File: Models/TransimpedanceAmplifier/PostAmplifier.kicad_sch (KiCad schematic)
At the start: 18 parts, among them J1 Conn_01x02_Pin, J7 Conn_01x02_Pin, J8 Conn_01x02_Pin, Q3 Q_PNP, Q4 Q_NPN, U6 OP37G

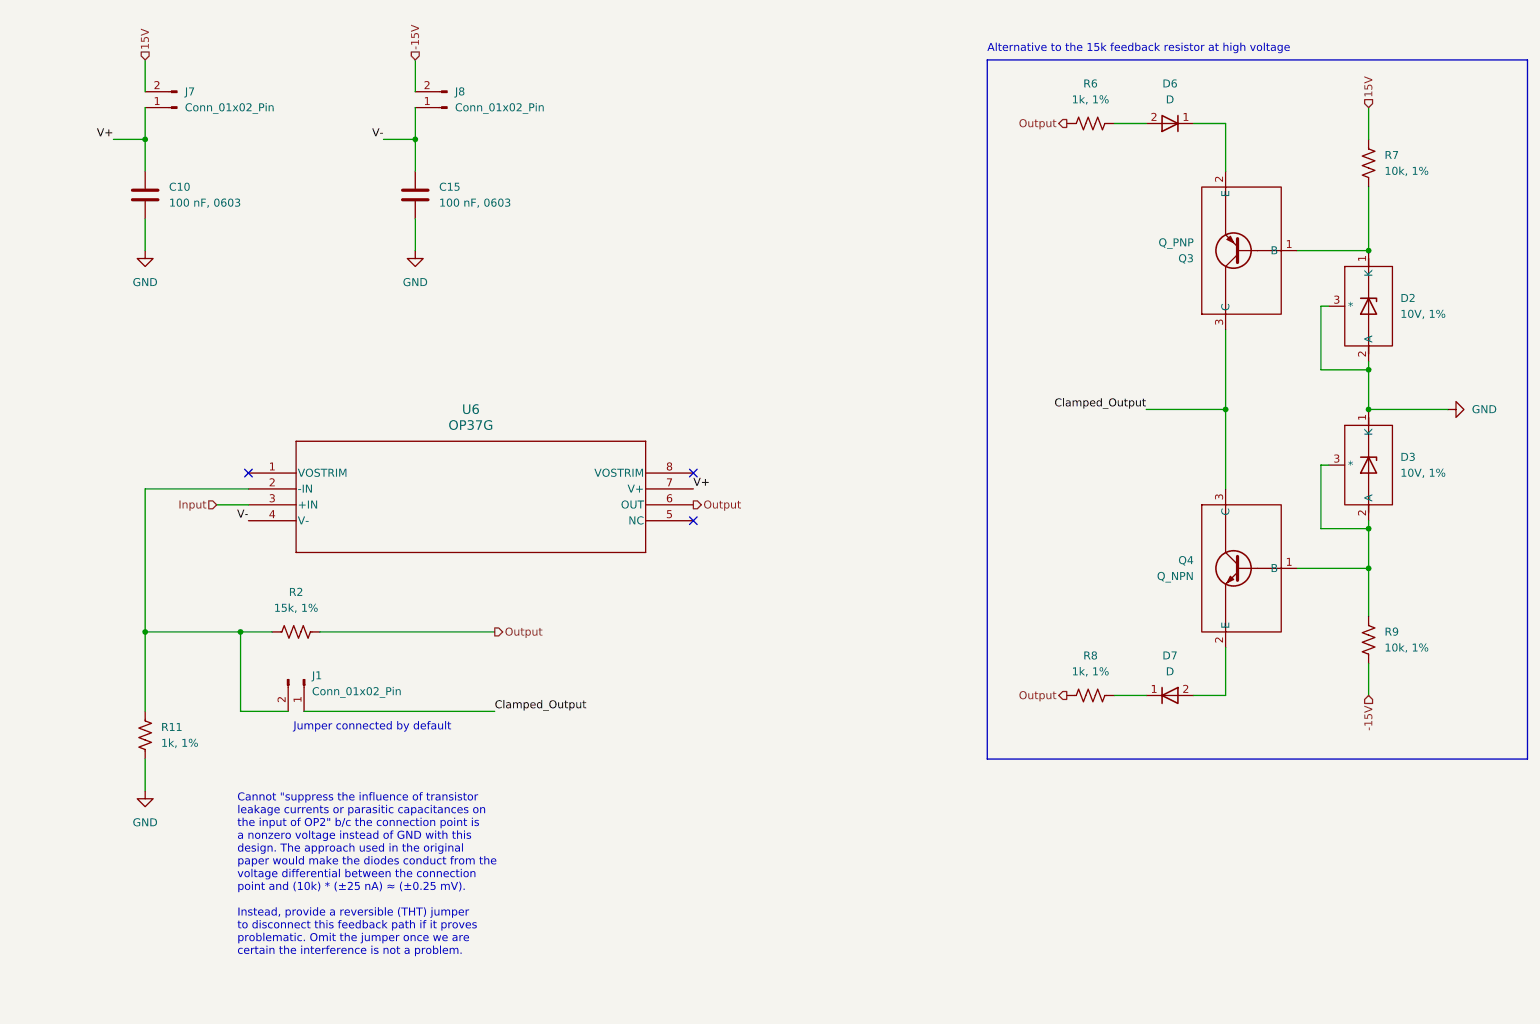
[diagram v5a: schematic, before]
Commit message: Overhauled all of the annotations
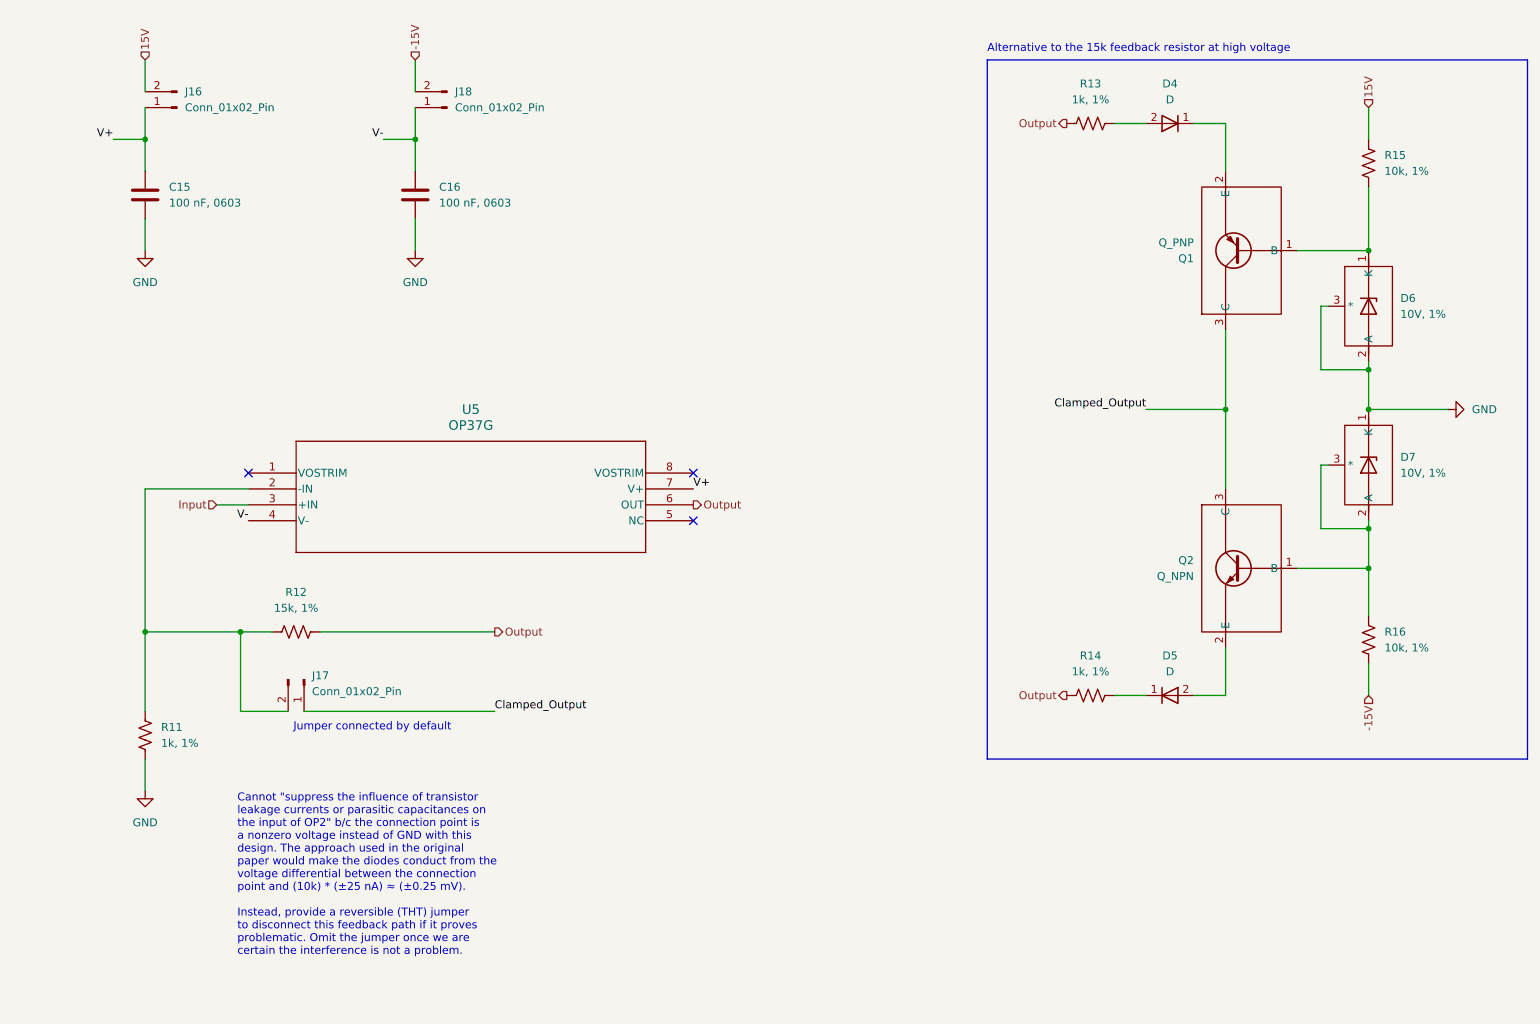
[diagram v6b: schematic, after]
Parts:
- renumbered C10 to C15, C15 to C16, D6 to D4, D7 to D5, D2 to D6, D3 to D7, J7 to J16, J1 to J17, J8 to J18, Q3 to Q1, Q4 to Q2, R2 to R12, R6 to R13, R8 to R14, R7 to R15, R9 to R16, U6 to U5
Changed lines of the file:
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@@
 		(dnp no)
 		(fields_autoplaced yes)
-		(property "Reference" "D2"
+		(property "Reference" "D6"
 			(at 251.46 73.6599 0)
 			(effects
@@
 			(project ""
 				(path "/ec9f2ae3-e40d-40eb-9760-2b611ee8efd1/226b3d0c-9e45-4bcf-9bef-58938aee743e/1a19fcb8-2301-474b-810f-9788696a69a6"
-					(reference "D2")
+					(reference "D6")
 					(unit 1)
 				)
@@
 		(dnp no)
 		(fields_autoplaced yes)
-		(property "Reference" "#PWR025"
+		(property "Reference" "#PWR018"
 			(at 50.8 72.39 0)
 			(effects
@@
 			(project "TransimpedanceAmplifier"
 				(path "/ec9f2ae3-e40d-40eb-9760-2b611ee8efd1/226b3d0c-9e45-4bcf-9bef-58938aee743e/1a19fcb8-2301-474b-810f-9788696a69a6"
-					(reference "#PWR025")
+					(reference "#PWR018")
 					(unit 1)
 				)
@@
 		(dnp no)
 		(fields_autoplaced yes)
-		(property "Reference" "R7"
+		(property "Reference" "R15"
 			(at 248.92 50.7999 0)
 			(effects
@@
 			(project "TransimpedanceAmplifier"
 				(path "/ec9f2ae3-e40d-40eb-9760-2b611ee8efd1/226b3d0c-9e45-4bcf-9bef-58938aee743e/1a19fcb8-2301-474b-810f-9788696a69a6"
-					(reference "R7")
+					(reference "R15")
 					(unit 1)
 				)
@@
 		(dnp no)
 		(fields_autoplaced yes)
-		(property "Reference" "J7"
+		(property "Reference" "J16"
 			(at 57.15 40.6399 0)
 			(effects
@@
 			(project "TransimpedanceAmplifier"
 				(path "/ec9f2ae3-e40d-40eb-9760-2b611ee8efd1/226b3d0c-9e45-4bcf-9bef-58938aee743e/1a19fcb8-2301-474b-810f-9788696a69a6"
-					(reference "J7")
+					(reference "J16")
 					(unit 1)
 				)
@@
 		(dnp no)
 		(fields_autoplaced yes)
-		(property "Reference" "C10"
+		(property "Reference" "C15"
 			(at 54.61 55.8799 0)
 			(effects
@@
 			(project "TransimpedanceAmplifier"
 				(path "/ec9f2ae3-e40d-40eb-9760-2b611ee8efd1/226b3d0c-9e45-4bcf-9bef-58938aee743e/1a19fcb8-2301-474b-810f-9788696a69a6"
-					(reference "C10")
+					(reference "C15")
 					(unit 1)
 				)
@@
 		(dnp no)
 		(fields_autoplaced yes)
-		(property "Reference" "#PWR02"
+		(property "Reference" "#PWR021"
 			(at 265.43 91.44 0)
 			(effects
@@
 			(project ""
 				(path "/ec9f2ae3-e40d-40eb-9760-2b611ee8efd1/226b3d0c-9e45-4bcf-9bef-58938aee743e/1a19fcb8-2301-474b-810f-9788696a69a6"
-					(reference "#PWR02")
+					(reference "#PWR021")
 					(unit 1)
 				)
@@
 		(dnp no)
 		(fields_autoplaced yes)
-		(property "Reference" "R9"
+		(property "Reference" "R16"
 			(at 248.92 126.9999 0)
 			(effects
@@
 			(project ""
 				(path "/ec9f2ae3-e40d-40eb-9760-2b611ee8efd1/226b3d0c-9e45-4bcf-9bef-58938aee743e/1a19fcb8-2301-474b-810f-9788696a69a6"
-					(reference "R9")
+					(reference "R16")
 					(unit 1)
 				)
@@
 		(dnp no)
 		(fields_autoplaced yes)
-		(property "Reference" "D6"
+		(property "Reference" "D4"
 			(at 214.63 39.37 0)
 			(effects
@@
 			(project "TransimpedanceAmplifier"
 				(path "/ec9f2ae3-e40d-40eb-9760-2b611ee8efd1/226b3d0c-9e45-4bcf-9bef-58938aee743e/1a19fcb8-2301-474b-810f-9788696a69a6"
-					(reference "D6")
+					(reference "D4")
 					(unit 1)
 				)
@@
 		(dnp no)
 		(fields_autoplaced yes)
-		(property "Reference" "#PWR026"
+		(property "Reference" "#PWR020"
 			(at 93.98 72.39 0)
 			(effects
@@
 			(project "TransimpedanceAmplifier"
 				(path "/ec9f2ae3-e40d-40eb-9760-2b611ee8efd1/226b3d0c-9e45-4bcf-9bef-58938aee743e/1a19fcb8-2301-474b-810f-9788696a69a6"
-					(reference "#PWR026")
+					(reference "#PWR020")
 					(unit 1)
 				)
@@
 		(dnp no)
 		(fields_autoplaced yes)
-		(property "Reference" "R8"
+		(property "Reference" "R14"
 			(at 201.93 130.81 90)
 			(effects
@@
 			(project ""
 				(path "/ec9f2ae3-e40d-40eb-9760-2b611ee8efd1/226b3d0c-9e45-4bcf-9bef-58938aee743e/1a19fcb8-2301-474b-810f-9788696a69a6"
-					(reference "R8")
+					(reference "R14")
 					(unit 1)
 				)
@@
 		(dnp no)
 		(fields_autoplaced yes)
-		(property "Reference" "U6"
+		(property "Reference" "U5"
 			(at 102.87 91.44 0)
 			(effects
@@
 			(project ""
 				(path "/ec9f2ae3-e40d-40eb-9760-2b611ee8efd1/226b3d0c-9e45-4bcf-9bef-58938aee743e/1a19fcb8-2301-474b-810f-9788696a69a6"
-					(reference "U6")
+					(reference "U5")
 					(unit 1)
 				)
@@
 		(dnp no)
 		(fields_autoplaced yes)
-		(property "Reference" "J1"
+		(property "Reference" "J17"
 			(at 77.47 133.9849 90)
 			(effects
@@
 			(project ""
 				(path "/ec9f2ae3-e40d-40eb-9760-2b611ee8efd1/226b3d0c-9e45-4bcf-9bef-58938aee743e/1a19fcb8-2301-474b-810f-9788696a69a6"
-					(reference "J1")
+					(reference "J17")
 					(unit 1)
 				)
@@
 		(on_board yes)
 		(dnp no)
-		(property "Reference" "Q3"
+		(property "Reference" "Q1"
 			(at 218.44 67.3101 0)
 			(effects
@@
 			(project ""
 				(path "/ec9f2ae3-e40d-40eb-9760-2b611ee8efd1/226b3d0c-9e45-4bcf-9bef-58938aee743e/1a19fcb8-2301-474b-810f-9788696a69a6"
-					(reference "Q3")
+					(reference "Q1")
 					(unit 1)
 				)
@@
 		(on_board yes)
 		(dnp no)
-		(property "Reference" "Q4"
+		(property "Reference" "Q2"
 			(at 218.44 115.5699 0)
 			(effects
@@
 			(project ""
 				(path "/ec9f2ae3-e40d-40eb-9760-2b611ee8efd1/226b3d0c-9e45-4bcf-9bef-58938aee743e/1a19fcb8-2301-474b-810f-9788696a69a6"
-					(reference "Q4")
+					(reference "Q2")
 					(unit 1)
 				)
@@
 		(dnp no)
 		(fields_autoplaced yes)
-		(property "Reference" "J8"
+		(property "Reference" "J18"
 			(at 100.33 40.6399 0)
 			(effects
@@
 			(project "TransimpedanceAmplifier"
 				(path "/ec9f2ae3-e40d-40eb-9760-2b611ee8efd1/226b3d0c-9e45-4bcf-9bef-58938aee743e/1a19fcb8-2301-474b-810f-9788696a69a6"
-					(reference "J8")
+					(reference "J18")
 					(unit 1)
 				)
@@
 		(dnp no)
 		(fields_autoplaced yes)
-		(property "Reference" "D7"
+		(property "Reference" "D5"
 			(at 214.63 130.81 0)
 			(effects
@@
 			(project "TransimpedanceAmplifier"
 				(path "/ec9f2ae3-e40d-40eb-9760-2b611ee8efd1/226b3d0c-9e45-4bcf-9bef-58938aee743e/1a19fcb8-2301-474b-810f-9788696a69a6"
-					(reference "D7")
+					(reference "D5")
 					(unit 1)
 				)
@@
 		(dnp no)
 		(fields_autoplaced yes)
-		(property "Reference" "C15"
+		(property "Reference" "C16"
 			(at 97.79 55.8799 0)
 			(effects
@@
 			(project "TransimpedanceAmplifier"
 				(path "/ec9f2ae3-e40d-40eb-9760-2b611ee8efd1/226b3d0c-9e45-4bcf-9bef-58938aee743e/1a19fcb8-2301-474b-810f-9788696a69a6"
-					(reference "C15")
+					(reference "C16")
 					(unit 1)
 				)
@@
 		(dnp no)
 		(fields_autoplaced yes)
-		(property "Reference" "R6"
+		(property "Reference" "R13"
 			(at 201.93 39.37 90)
 			(effects
@@
 			(project ""
 				(path "/ec9f2ae3-e40d-40eb-9760-2b611ee8efd1/226b3d0c-9e45-4bcf-9bef-58938aee743e/1a19fcb8-2301-474b-810f-9788696a69a6"
-					(reference "R6")
+					(reference "R13")
 					(unit 1)
 				)
@@
 		(dnp no)
 		(fields_autoplaced yes)
-		(property "Reference" "#PWR04"
+		(property "Reference" "#PWR019"
 			(at 50.8 158.75 0)
 			(effects
@@
 			(project ""
 				(path "/ec9f2ae3-e40d-40eb-9760-2b611ee8efd1/226b3d0c-9e45-4bcf-9bef-58938aee743e/1a19fcb8-2301-474b-810f-9788696a69a6"
-					(reference "#PWR04")
+					(reference "#PWR019")
 					(unit 1)
 				)
@@
 		(dnp no)
 		(fields_autoplaced yes)
-		(property "Reference" "R2"
+		(property "Reference" "R12"
 			(at 74.93 120.65 90)
 			(effects
@@
 			(project "TransimpedanceAmplifier"
 				(path "/ec9f2ae3-e40d-40eb-9760-2b611ee8efd1/226b3d0c-9e45-4bcf-9bef-58938aee743e/1a19fcb8-2301-474b-810f-9788696a69a6"
-					(reference "R2")
+					(reference "R12")
 					(unit 1)
 				)
@@
 		(dnp no)
 		(fields_autoplaced yes)
-		(property "Reference" "D3"
+		(property "Reference" "D7"
 			(at 251.46 99.0599 0)
 			(effects
@@
 			(project ""
 				(path "/ec9f2ae3-e40d-40eb-9760-2b611ee8efd1/226b3d0c-9e45-4bcf-9bef-58938aee743e/1a19fcb8-2301-474b-810f-9788696a69a6"
-					(reference "D3")
-					(unit 1)
-				)
+					(reference "D7")
+					(unit 1)
+				)

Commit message: Completely fixed the batteries
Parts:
- renumbered J18 to J10, J16 to J8, J17 to J9
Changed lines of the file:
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@@
 		(dnp no)
 		(fields_autoplaced yes)
-		(property "Reference" "J16"
+		(property "Reference" "J8"
 			(at 57.15 40.6399 0)
 			(effects
@@
 			(project "TransimpedanceAmplifier"
 				(path "/ec9f2ae3-e40d-40eb-9760-2b611ee8efd1/226b3d0c-9e45-4bcf-9bef-58938aee743e/1a19fcb8-2301-474b-810f-9788696a69a6"
-					(reference "J16")
+					(reference "J8")
 					(unit 1)
 				)
@@
 		(dnp no)
 		(fields_autoplaced yes)
-		(property "Reference" "J17"
+		(property "Reference" "J9"
 			(at 77.47 133.9849 90)
 			(effects
@@
 			(project ""
 				(path "/ec9f2ae3-e40d-40eb-9760-2b611ee8efd1/226b3d0c-9e45-4bcf-9bef-58938aee743e/1a19fcb8-2301-474b-810f-9788696a69a6"
-					(reference "J17")
+					(reference "J9")
 					(unit 1)
 				)
@@
 		(dnp no)
 		(fields_autoplaced yes)
-		(property "Reference" "J18"
+		(property "Reference" "J10"
 			(at 100.33 40.6399 0)
 			(effects
@@
 			(project "TransimpedanceAmplifier"
 				(path "/ec9f2ae3-e40d-40eb-9760-2b611ee8efd1/226b3d0c-9e45-4bcf-9bef-58938aee743e/1a19fcb8-2301-474b-810f-9788696a69a6"
-					(reference "J18")
-					(unit 1)
-				)
+					(reference "J10")
+					(unit 1)
+				)

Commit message: Finalized the last detail of the schematic
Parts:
- renumbered R11 to R12, R12 to R13, R13 to R14, R14 to R15, R15 to R16, R16 to R17
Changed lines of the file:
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@@
 		(dnp no)
 		(fields_autoplaced yes)
-		(property "Reference" "R11"
+		(property "Reference" "R12"
 			(at 53.34 142.2399 0)
 			(effects
@@
 			(project "TransimpedanceAmplifier"
 				(path "/ec9f2ae3-e40d-40eb-9760-2b611ee8efd1/226b3d0c-9e45-4bcf-9bef-58938aee743e/1a19fcb8-2301-474b-810f-9788696a69a6"
-					(reference "R11")
+					(reference "R12")
 					(unit 1)
 				)
@@
 		(dnp no)
 		(fields_autoplaced yes)
-		(property "Reference" "R15"
+		(property "Reference" "R16"
 			(at 248.92 50.7999 0)
 			(effects
@@
 			(project "TransimpedanceAmplifier"
 				(path "/ec9f2ae3-e40d-40eb-9760-2b611ee8efd1/226b3d0c-9e45-4bcf-9bef-58938aee743e/1a19fcb8-2301-474b-810f-9788696a69a6"
-					(reference "R15")
+					(reference "R16")
 					(unit 1)
 				)
@@
 		(dnp no)
 		(fields_autoplaced yes)
-		(property "Reference" "R16"
+		(property "Reference" "R17"
 			(at 248.92 126.9999 0)
 			(effects
@@
 			(project ""
 				(path "/ec9f2ae3-e40d-40eb-9760-2b611ee8efd1/226b3d0c-9e45-4bcf-9bef-58938aee743e/1a19fcb8-2301-474b-810f-9788696a69a6"
-					(reference "R16")
+					(reference "R17")
 					(unit 1)
 				)
@@
 		(dnp no)
 		(fields_autoplaced yes)
-		(property "Reference" "R14"
+		(property "Reference" "R15"
 			(at 201.93 130.81 90)
 			(effects
@@
 			(project ""
 				(path "/ec9f2ae3-e40d-40eb-9760-2b611ee8efd1/226b3d0c-9e45-4bcf-9bef-58938aee743e/1a19fcb8-2301-474b-810f-9788696a69a6"
-					(reference "R14")
+					(reference "R15")
 					(unit 1)
 				)
@@
 		(dnp no)
 		(fields_autoplaced yes)
-		(property "Reference" "R13"
+		(property "Reference" "R14"
 			(at 201.93 39.37 90)
 			(effects
@@
 			(project ""
 				(path "/ec9f2ae3-e40d-40eb-9760-2b611ee8efd1/226b3d0c-9e45-4bcf-9bef-58938aee743e/1a19fcb8-2301-474b-810f-9788696a69a6"
-					(reference "R13")
+					(reference "R14")
 					(unit 1)
 				)
@@
 		(dnp no)
 		(fields_autoplaced yes)
-		(property "Reference" "R12"
+		(property "Reference" "R13"
 			(at 74.93 120.65 90)
 			(effects
@@
 			(project "TransimpedanceAmplifier"
 				(path "/ec9f2ae3-e40d-40eb-9760-2b611ee8efd1/226b3d0c-9e45-4bcf-9bef-58938aee743e/1a19fcb8-2301-474b-810f-9788696a69a6"
-					(reference "R12")
-					(unit 1)
-				)
+					(reference "R13")
+					(unit 1)
+				)
